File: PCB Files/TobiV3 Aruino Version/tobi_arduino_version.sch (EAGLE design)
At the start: 45 parts, among them M1 M1_M2, M2 M1_M2, M3 DF11-4PIN, M4 DF11-4PIN, M5 DF11-4PIN, M6 DF11-4PIN

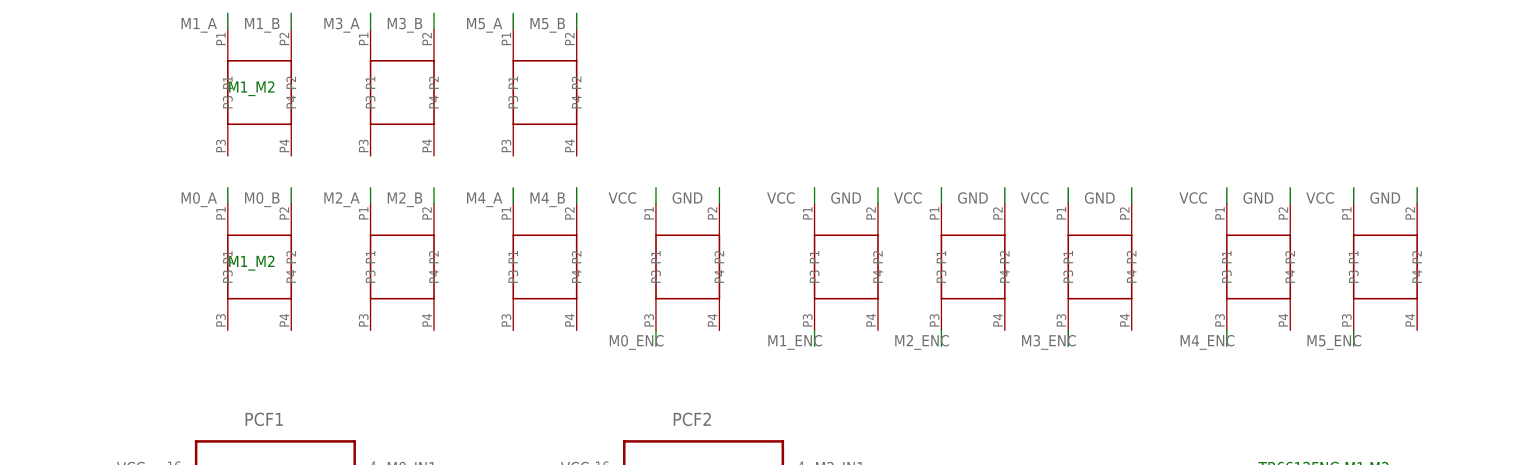
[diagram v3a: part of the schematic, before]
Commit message: simple headers for encoders and motors
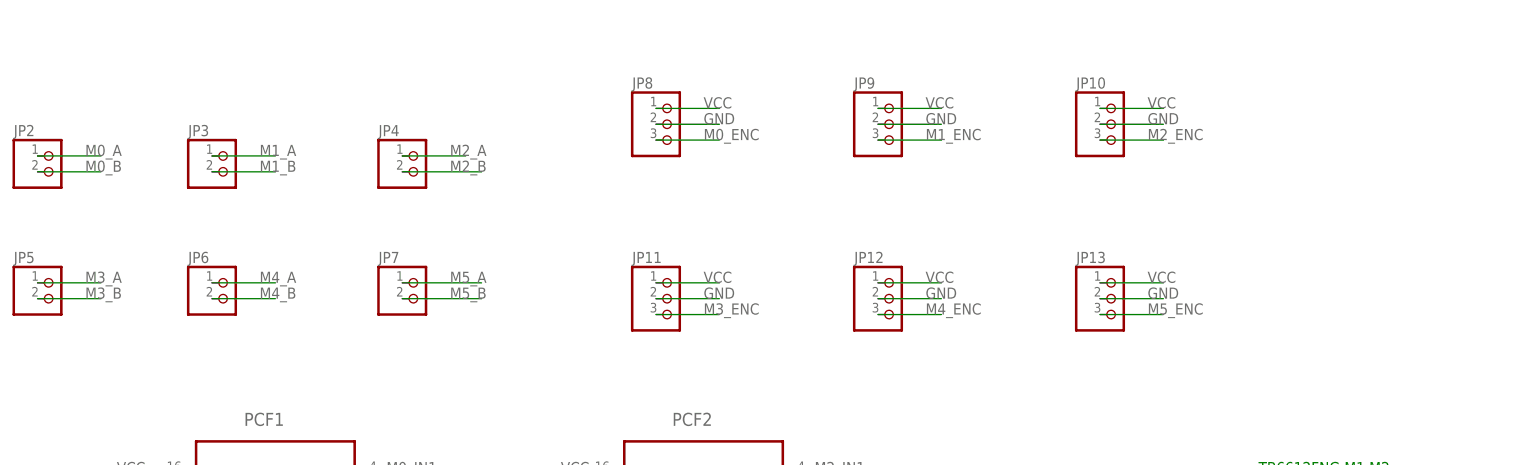
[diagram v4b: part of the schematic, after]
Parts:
- removed ENC1, ENC2, ENC3, ENC4, ENC5, ENC6, M3, M4, M5, M6: DF11-4PIN, Gavin:DF11-4PIN
- removed M1, M2: M1_M2, Gavin:DF11-4PIN
- added JP10, JP11, JP12, JP13, JP8, JP9: (no value), pinhead:PINHD-1X3
- added JP2, JP3, JP4, JP5, JP6, JP7: (no value), pinhead:PINHD-1X2
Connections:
- net GND: now also JP10.2, JP11.2, JP12.2, JP13.2, JP8.2, JP9.2; no longer ENC1.P2, ENC2.P2, ENC3.P2, ENC4.P2, ENC5.P2, ENC6.P2
- net M0_A: now also JP2.1; no longer M1.P1
- net M0_B: now also JP2.2; no longer M1.P2
- net M0_ENC: now also JP8.3; no longer ENC1.P3
- net M1_A: now also JP3.1; no longer M2.P1
- net M1_B: now also JP3.2; no longer M2.P2
- net M1_ENC: now also JP9.3; no longer ENC2.P3
- net M2_A: now also JP4.1; no longer M3.P1
- net M2_B: now also JP4.2; no longer M3.P2
- net M2_ENC: now also JP10.3; no longer ENC3.P3
- net M3_A: now also JP5.1; no longer M4.P1
- net M3_B: now also JP5.2; no longer M4.P2
- net M3_ENC: now also JP11.3; no longer ENC4.P3
- net M4_A: now also JP6.1; no longer M5.P1
- net M4_B: now also JP6.2; no longer M5.P2
- net M4_ENC: now also JP12.3; no longer ENC5.P3
- net M5_A: now also JP7.1; no longer M6.P1
- net M5_B: now also JP7.2; no longer M6.P2
- net M5_ENC: now also JP13.3; no longer ENC6.P3
- net VCC: now also JP10.1, JP11.1, JP12.1, JP13.1, JP8.1, JP9.1; no longer ENC1.P1, ENC2.P1, ENC3.P1, ENC4.P1, ENC5.P1, ENC6.P1
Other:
- note removed: "M1_M2"

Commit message: first shot at positioning components
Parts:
- renumbered JP10 to M2_ENC, JP11 to M3_ENC, JP12 to M4_ENC, JP13 to M5_ENC, JP2 to MOT_0, JP3 to MOT_1, JP4 to MOT_2, JP5 to MOT_3, JP6 to MOT_4, JP7 to MOT_5, JP8 to M0_ENC, JP9 to M1_ENC
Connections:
- new net N$1: LED0.A, R_LED0.1
- new net N$2: LED1.A, R_LED1.1
- new net N$3: LED2.A, R_LED2.1
- new net N$4: LED3.A, R_LED3.1
- new net N$5: LED4.A, R_LED4.1
- new net N$6: LED5.A, R_LED5.1
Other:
- moved on the sheet: LED0, LED1, LED2, LED3, LED4, LED5, R_LED0, R_LED1, R_LED2, R_LED3, R_LED4, R_LED5

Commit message: reconciled some nets
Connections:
- removed net V_IN: POWR-PLUG.POW
- net V_MOT: now also POWR-PLUG.POW
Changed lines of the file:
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@@
 <label x="60.96" y="66.04" size="1.778" layer="95"/>
+</segment>
+<segment>
+<pinref part="POWR-PLUG" gate="G$1" pin="POW"/>
+<wire x1="7.62" y1="-2.54" x2="0" y2="-2.54" width="0.1524" layer="91"/>
+<label x="-2.54" y="-2.54" size="1.778" layer="95"/>
 </segment>
 </net>
@@
 </segment>
 </net>
-<net name="V_IN" class="0">
-<segment>
-<pinref part="POWR-PLUG" gate="G$1" pin="POW"/>
-<wire x1="7.62" y1="-2.54" x2="0" y2="-2.54" width="0.1524" layer="91"/>
-<label x="-2.54" y="-2.54" size="1.778" layer="95"/>
-</segment>
-</net>

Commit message: fix to motor 5 net
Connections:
- net M4_B: no longer DRIVER3.BO2
- net M5_B: now also DRIVER3.BO2

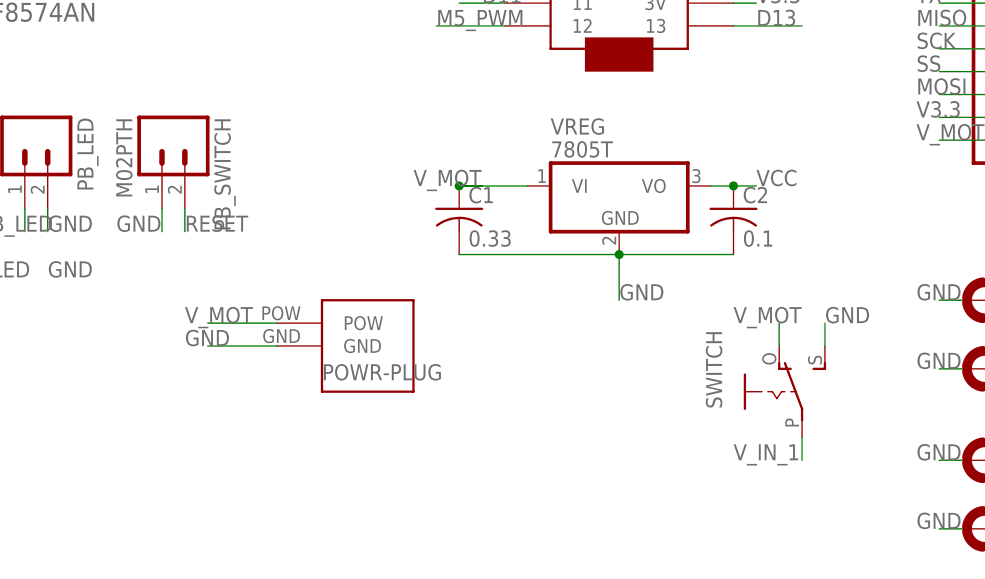
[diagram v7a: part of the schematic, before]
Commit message: add thick traces for battery voltage, motor voltage, sda, scl
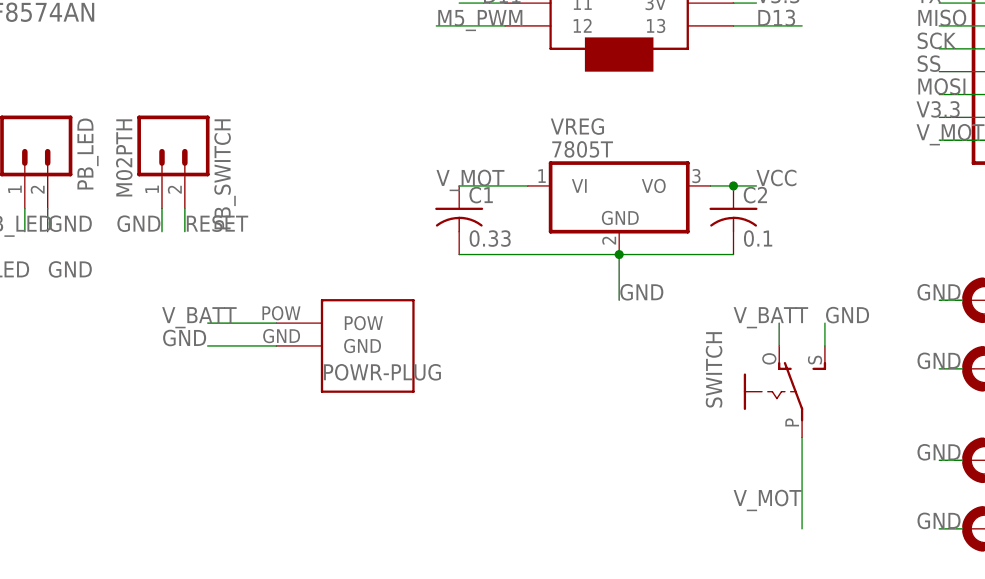
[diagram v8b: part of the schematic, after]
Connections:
- removed net V_IN_1: SWITCH.P
- new net V_BATT: POWR-PLUG.POW, SWITCH.O
- net V_MOT: now also SWITCH.P; no longer POWR-PLUG.POW, SWITCH.O
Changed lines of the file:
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@@
 <pinref part="POWR-PLUG" gate="G$1" pin="GND"/>
 <wire x1="7.62" y1="-5.08" x2="0" y2="-5.08" width="0.1524" layer="91"/>
-<label x="-2.54" y="-5.08" size="1.778" layer="95"/>
+<label x="-5.08" y="-5.08" size="1.778" layer="95"/>
 </segment>
 <segment>
@@
 <net name="V_MOT" class="0">
 <segment>
-<pinref part="VREG" gate="A1" pin="VI"/>
-<pinref part="C1" gate="G$1" pin="1"/>
-<wire x1="27.94" y1="12.7" x2="30.48" y2="12.7" width="0.1524" layer="91"/>
-<junction x="27.94" y="12.7"/>
-<label x="22.86" y="12.7" size="1.778" layer="95"/>
-<wire x1="27.94" y1="12.7" x2="35.56" y2="12.7" width="0.1524" layer="91"/>
-</segment>
-<segment>
 <pinref part="DRIVER1" gate="G$1" pin="VMOT"/>
 <wire x1="129.54" y1="101.6" x2="127" y2="101.6" width="0.1524" layer="91"/>
@@
 </segment>
 <segment>
-<pinref part="SWITCH" gate="1" pin="O"/>
-<wire x1="63.5" y1="-5.08" x2="63.5" y2="-2.54" width="0.1524" layer="91"/>
-<label x="58.42" y="-2.54" size="1.778" layer="95"/>
-</segment>
-<segment>
 <pinref part="JP1" gate="A" pin="20"/>
 <wire x1="88.9" y1="17.78" x2="81.28" y2="17.78" width="0.1524" layer="91"/>
@@
 </segment>
 <segment>
-<pinref part="POWR-PLUG" gate="G$1" pin="POW"/>
-<wire x1="7.62" y1="-2.54" x2="0" y2="-2.54" width="0.1524" layer="91"/>
-<label x="-2.54" y="-2.54" size="1.778" layer="95"/>
+<pinref part="VREG" gate="A1" pin="VI"/>
+<pinref part="C1" gate="G$1" pin="1"/>
+<wire x1="35.56" y1="12.7" x2="27.94" y2="12.7" width="0.1524" layer="91"/>
+<label x="25.4" y="12.7" size="1.778" layer="95"/>
+</segment>
+<segment>
+<pinref part="SWITCH" gate="1" pin="P"/>
+<wire x1="66.04" y1="-15.24" x2="66.04" y2="-25.4" width="0.1524" layer="91"/>
+<label x="58.42" y="-22.86" size="1.778" layer="95"/>
 </segment>
 </net>
@@
 </segment>
 </net>
-<net name="V_IN_1" class="0">
-<segment>
-<pinref part="SWITCH" gate="1" pin="P"/>
-<wire x1="66.04" y1="-15.24" x2="66.04" y2="-17.78" width="0.1524" layer="91"/>
-<label x="58.42" y="-17.78" size="1.778" layer="95"/>
-</segment>
-</net>
 <net name="LED4" class="0">
 <segment>
@@
 </segment>
 </net>
+<net name="V_BATT" class="0">
+<segment>
+<pinref part="POWR-PLUG" gate="G$1" pin="POW"/>
+<wire x1="7.62" y1="-2.54" x2="0" y2="-2.54" width="0.1524" layer="91"/>
+<label x="-5.08" y="-2.54" size="1.778" layer="95"/>
+</segment>
+<segment>
+<pinref part="SWITCH" gate="1" pin="O"/>
+<wire x1="63.5" y1="-5.08" x2="63.5" y2="-2.54" width="0.1524" layer="91"/>
+<label x="58.42" y="-2.54" size="1.778" layer="95"/>
+</segment>
+</net>
